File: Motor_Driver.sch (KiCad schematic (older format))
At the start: 42 parts, among them CN3 CONN_HEADER_R_A_2POS_2.5MM, Q14 AOD4185, Q5 2N7002BK, Q6 2N7002BK, Q7 2N7002BK, U7 LMC6772AIMX, U8 VNH5019ATR-E

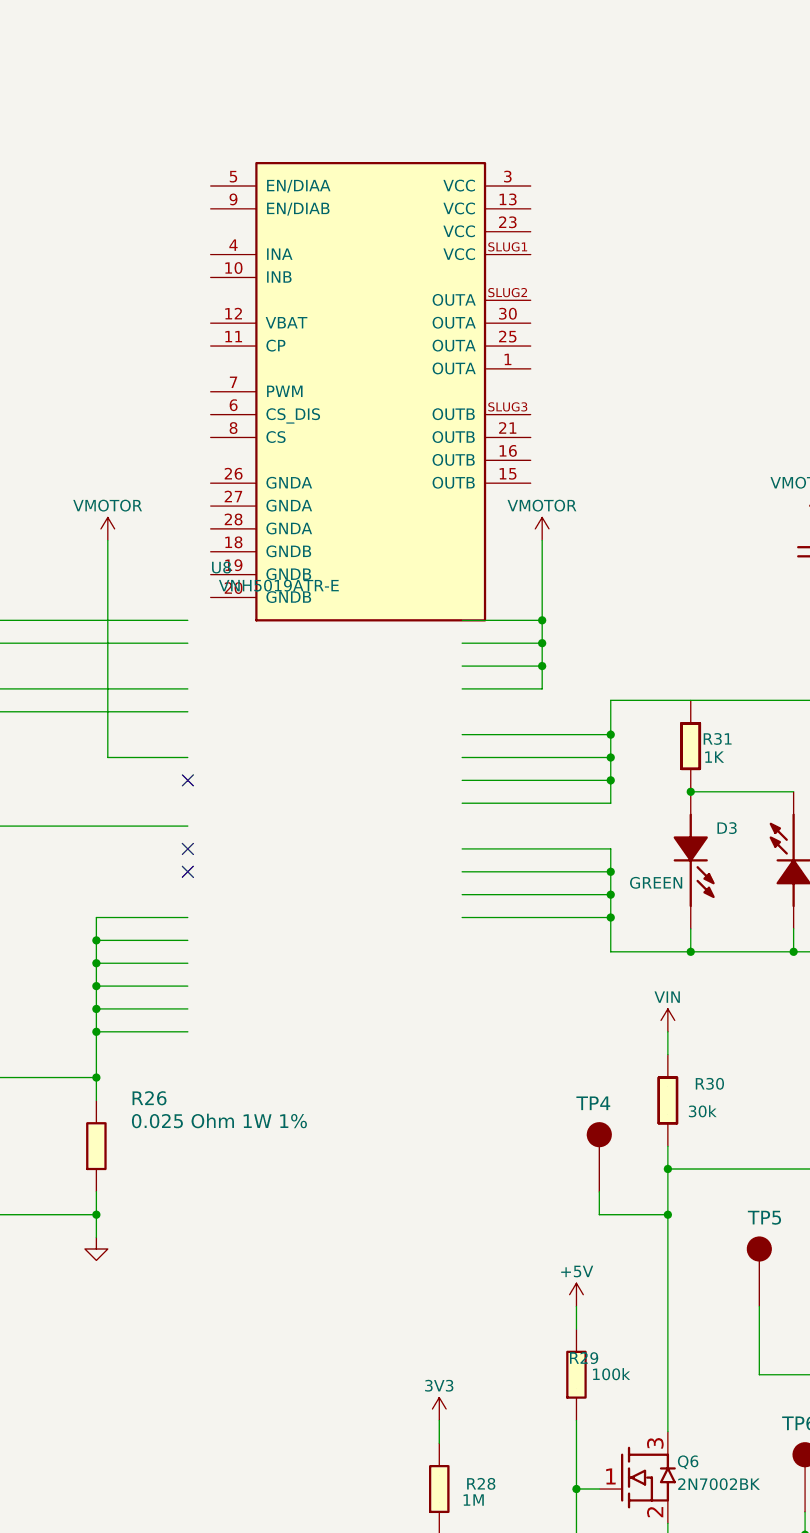
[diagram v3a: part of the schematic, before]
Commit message: Tweaked some issues on the battery charger page.
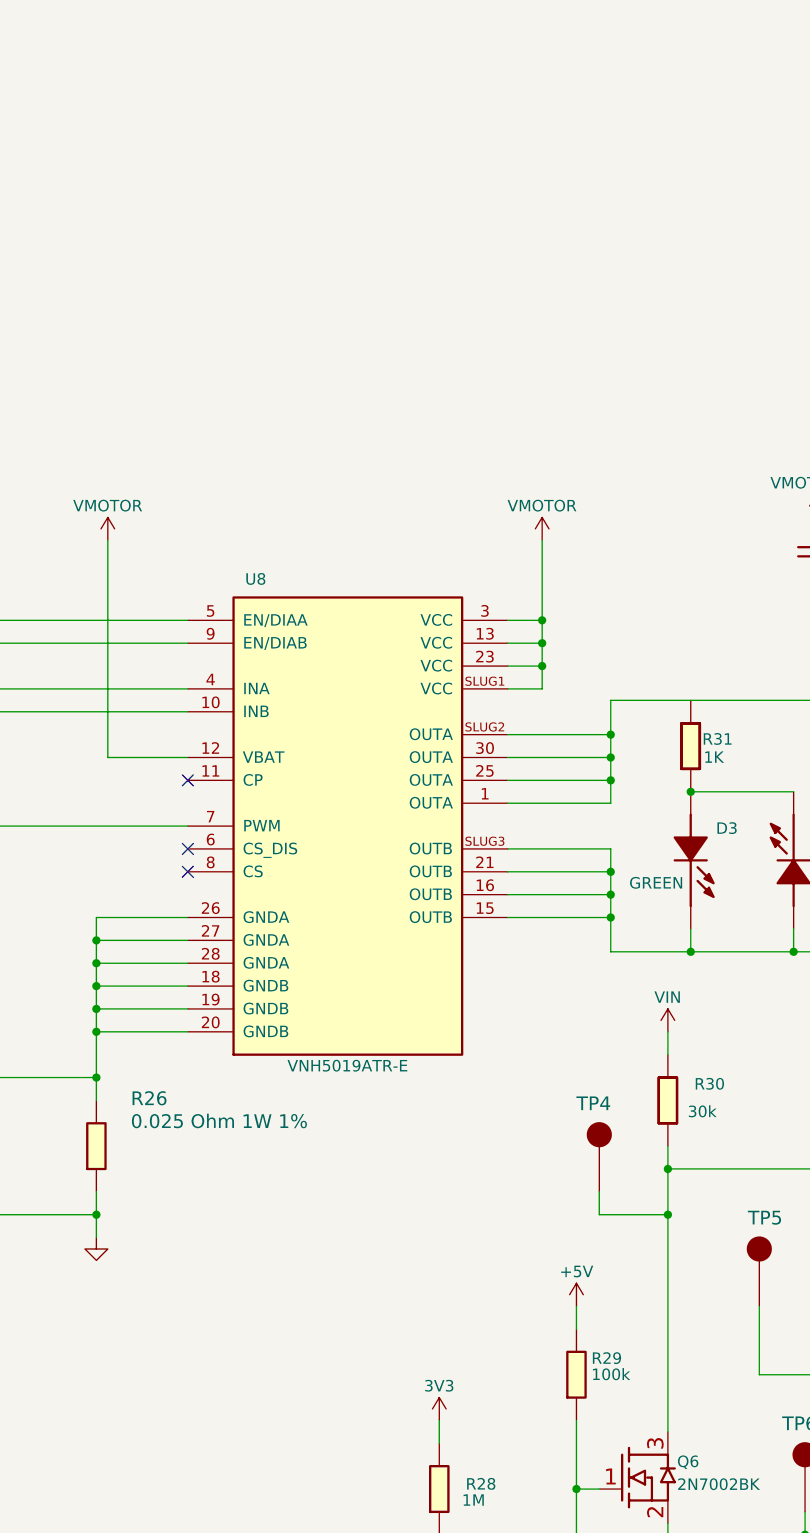
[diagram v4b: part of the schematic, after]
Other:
- moved on the sheet: U8
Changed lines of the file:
@@
 	4400 800  4400 1750
 Wire Wire Line
-	6600 2450 5950 2450
-Wire Wire Line
 	6600 2600 6600 2450
 Wire Wire Line
@@
 	8700 2050 8700 2600
 Wire Wire Line
-	6600 2350 5950 2350
-Wire Wire Line
-	6600 2250 5950 2250
-Wire Wire Line
-	6600 2150 5950 2150
-Wire Wire Line
 	6600 2250 6600 2150
 Wire Wire Line
@@
 	6600 2450 6600 2350
 Wire Wire Line
-	6600 1950 5950 1950
-Wire Wire Line
 	6600 1850 6600 1950
 Wire Wire Line
@@
 	6600 1650 6600 1750
 Wire Wire Line
-	6600 1850 5950 1850
-Wire Wire Line
-	6600 1750 5950 1750
-Wire Wire Line
-	6600 1650 5950 1650
-Wire Wire Line
 	6600 1500 6600 1650
 Wire Wire Line
 	8700 1950 8700 1500
 Wire Wire Line
-	6300 1450 5950 1450
-Wire Wire Line
 	6300 1350 6300 1450
 Wire Wire Line
@@
 Wire Wire Line
 	6300 800  6300 1150
-Wire Wire Line
-	6300 1350 5950 1350
-Wire Wire Line
-	6300 1250 5950 1250
-Wire Wire Line
-	6300 1150 5950 1150
 Wire Wire Line
 	7500 1150 7500 1000
@@
 L OpenVent:VNH5019ATR-E U8
 U 1 1 5F8DD116
-P 4850 1050
-F 0 "U8" H 4850 1150 50  0000 L BNN
-F 1 "VNH5019ATR-E" H 5150 1100 50  0000 C CNN
-F 2 "Package_SO:ST_MultiPowerSO-30" H 4850 1050 50  0001 C CNN
-F 3 "http://www.st.com/content/ccc/resource/technical/document/datasheet/1c/26/60/a8/3e/70/4c/e1/CD00234623.pdf/files/CD00234623.pdf/jcr:content/translations/en.CD00234623.pdf" H 4850 1050 60  0001 C CNN
-F 4 "STMicroelectronics" H 4850 1050 50  0001 C CNN "Mfr"
-F 5 "VNH5019ATR-E" H 4850 1050 50  0001 C CNN "Mfr_PN"
-F 6 "IC MTR DRV 5.5-24V MULTIPWRSO-30" H 4850 1050 50  0001 C CNN "Desc"
-F 7 "Motor Driver Power MOSFET Parallel, PWM MultiPowerSO-30" H 4850 1050 50  0001 C CNN "Detailed"
-F 8 "DigiKey" H 4850 1050 50  0001 C CNN "DistName"
-F 9 "497-13073-2-ND" H 4850 1050 50  0001 C CNN "Dist_PN"
-	1    4850 1050
+P 4750 2950
+F 0 "U8" H 5000 4900 50  0000 L BNN
+F 1 "VNH5019ATR-E" H 5450 2800 50  0000 C CNN
+F 2 "Package_SO:ST_MultiPowerSO-30" H 4750 2950 50  0001 C CNN
+F 3 "http://www.st.com/content/ccc/resource/technical/document/datasheet/1c/26/60/a8/3e/70/4c/e1/CD00234623.pdf/files/CD00234623.pdf/jcr:content/translations/en.CD00234623.pdf" H 4750 2950 60  0001 C CNN
+F 4 "STMicroelectronics" H 4750 2950 50  0001 C CNN "Mfr"
+F 5 "VNH5019ATR-E" H 4750 2950 50  0001 C CNN "Mfr_PN"
+F 6 "IC MTR DRV 5.5-24V MULTIPWRSO-30" H 4750 2950 50  0001 C CNN "Desc"
+F 7 "Motor Driver Power MOSFET Parallel, PWM MultiPowerSO-30" H 4750 2950 50  0001 C CNN "Detailed"
+F 8 "DigiKey" H 4750 2950 50  0001 C CNN "DistName"
+F 9 "497-13073-2-ND" H 4750 2950 50  0001 C CNN "Dist_PN"
+	1    4750 2950
 	1    0    0    -1
 $EndComp
@@
 U 1 1 5F8DD0FC
 P 6350 4550
-F 0 "R29" V 6550 4350 50  0000 L BNN
+F 0 "R29" V 6550 4250 50  0000 L BNN
 F 1 "100K_0603_Chip_Resistor,_1%,_0.1W" V 6350 4400 50  0001 C CNN
 F 2 "Resistor_SMD:R_0603_1608Metric" H 6250 4410 50  0001 C CNN
@@
 	1    0    0    -1
 $EndComp
+Wire Wire Line
+	6300 1450 6150 1450
+Wire Wire Line
+	6600 1950 6150 1950
+Wire Wire Line
+	6600 2150 6150 2150
+Wire Wire Line
+	6300 1350 6150 1350
+Wire Wire Line
+	6300 1250 6150 1250
+Wire Wire Line
+	6300 1150 6150 1150
+Wire Wire Line
+	6600 2450 6150 2450
+Wire Wire Line
+	6600 2350 6150 2350
+Wire Wire Line
+	6600 2250 6150 2250
+Wire Wire Line
+	6600 1850 6150 1850
+Wire Wire Line
+	6600 1750 6150 1750
+Wire Wire Line
+	6600 1650 6150 1650
 $EndSCHEMATC

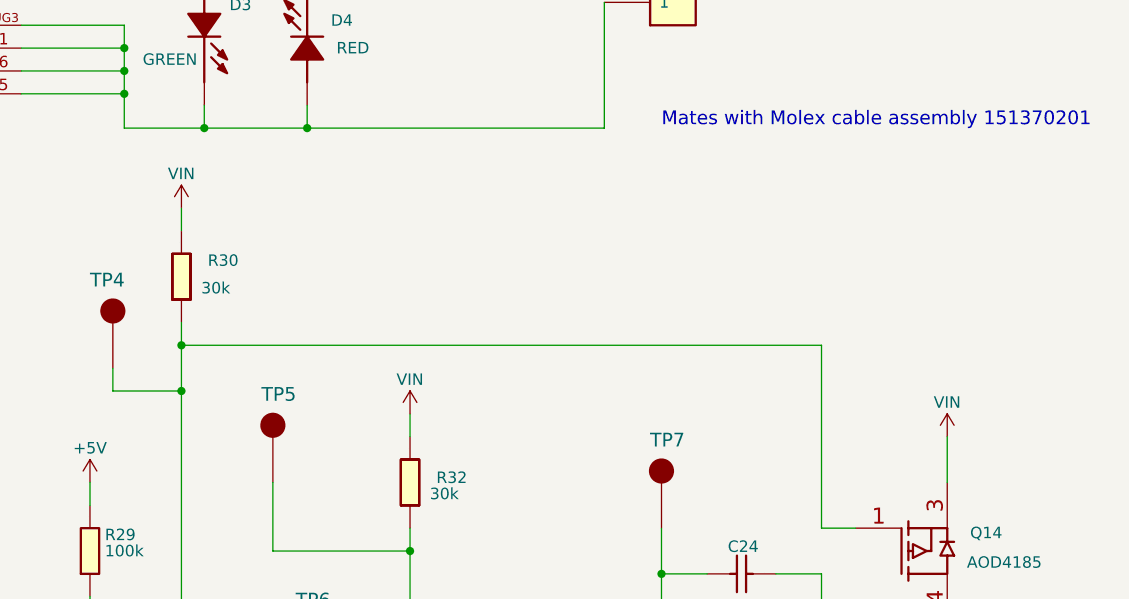
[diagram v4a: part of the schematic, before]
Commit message: Battery Charger page mostly finished, might want to think about what to do with the battery charging current signal (it's analog).
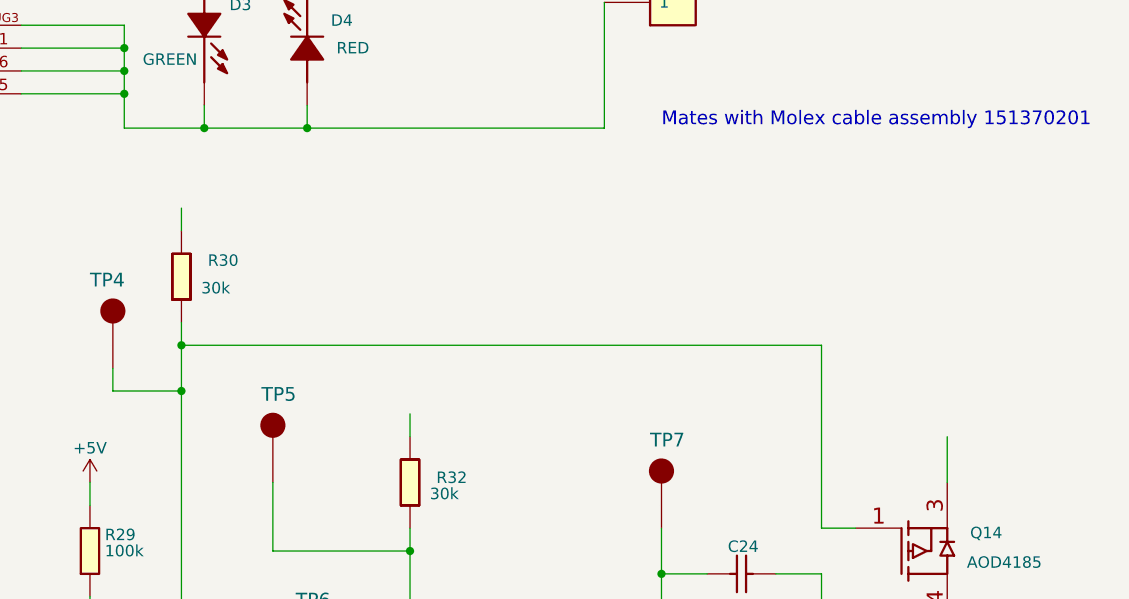
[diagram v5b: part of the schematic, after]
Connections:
- removed net VIN: Q14.3 (Source), R30.2, R32.2
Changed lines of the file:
@@
-$EndComp
-$Comp
-L OpenVent:VIN #VIN_02
-U 1 1 5F8DD127
-P 7850 3850
-F 0 "#VIN_02" H 7850 3850 20  0001 C CNN
-F 1 "VIN" H 7850 4000 50  0000 C CNN
-F 2 "" H 7850 3850 70  0000 C CNN
-F 3 "" H 7850 3850 70  0000 C CNN
-	1    7850 3850
-	1    0    0    -1
-$EndComp
-$Comp
-L OpenVent:VIN #VIN_03
-U 1 1 5F8DD126
-P 10200 3950
-F 0 "#VIN_03" H 10200 3950 20  0001 C CNN
-F 1 "VIN" H 10200 4100 50  0000 C CNN
-F 2 "" H 10200 3950 70  0000 C CNN
-F 3 "" H 10200 3950 70  0000 C CNN
-	1    10200 3950
-	1    0    0    -1
 $EndComp
 $Comp
@@
 	1    0    0    -1
 $EndComp
-$Comp
-L OpenVent:VIN #VIN_01
-U 1 1 5F8DD11E
-P 6850 2950
-F 0 "#VIN_01" H 6850 2950 20  0001 C CNN
-F 1 "VIN" H 6850 3100 50  0000 C CNN
-F 2 "" H 6850 2950 70  0000 C CNN
-F 3 "" H 6850 2950 70  0000 C CNN
-	1    6850 2950
-	1    0    0    -1
-$EndComp

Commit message: Split the design into two boards, main controller board and a power supply board.
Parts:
- removed C21: 470pF_0603_Ceramic_Capacitor,_5%,_100V,_C0G, Capacitor_SMD:C_0603_1608Metric, symbol OpenVent:470pF_0603_Ceramic_Capacitor,_5%,_100V,_C0G
- removed C22, C23: 1000uF_25V_Aluminium_SMD_Capacitor,_20%, Capacitor_SMD:CP_Elec_10x10, symbol OpenVent:1000uF_25V_Aluminium_SMD_Capacitor,_20%
- removed C24: 10nF_0603_Ceramic_Capacitor,_10%,_50V,_X7R-, Capacitor_SMD:C_0603_1608Metric, symbol OpenVent:10nF_0603_Ceramic_Capacitor,_10%,_50V,_X7R-
- removed CN3: CONN_HEADER_R_A_2POS_2.5MM, symbol OpenVent:CONN_HEADER_R_A_2POS_2.5MM
- removed D3: LED_GREEN_0603_SMD, LED_SMD:LED_0603_1608Metric, symbol OpenVent:LED_GREEN_0603_SMD
- removed D4: LED_Red_0603_SMD, LED_SMD:LED_0603_1608Metric, symbol OpenVent:LED_Red_0603_SMD
- removed D5: FSV20100V, Package_TO_SOT_SMD:TO-277A, symbol OpenVent:FSV20100V
- removed Q14: AOD4185, Package_TO_SOT_SMD:TO-252-2, symbol OpenVent:AOD4185
- removed Q5, Q6, Q7: 2N7002BK, Package_TO_SOT_SMD:SOT-23, symbol OpenVent:2N7002BK
- removed R16, R18, R27: 10k_0603_Chip_Resistor,_1%,_0.1W, Resistor_SMD:R_0603_1608Metric, symbol OpenVent:10k_0603_Chip_Resistor,_1%,_0.1W
- removed R17, R23: 215k_0603_Chip_Resistor,_1%,_0.1W, Resistor_SMD:R_0603_1608Metric, symbol OpenVent:215k_0603_Chip_Resistor,_1%,_0.1W
- removed R19, R20, R21, R22, R31: 1K_0603_Chip_Resistor,_1%,_0.1W, Resistor_SMD:R_0603_1608Metric, symbol OpenVent:1K_0603_Chip_Resistor,_1%,_0.1W
- removed R24, R25: 4k7_0603_Chip_Resistor,_1%,_0.1W, Resistor_SMD:R_0603_1608Metric, symbol OpenVent:4k7_0603_Chip_Resistor,_1%,_0.1W
- removed R26: 0.025 Ohm 1W 1%, Resistor_SMD:R_2010_5025Metric, symbol OpenVent:Resistor_2010_0.025OHM_sensing_1%_1W
- removed R28: 1M_0603_Chip_Resistor,_1%,_0.1W, Resistor_SMD:R_0603_1608Metric, symbol OpenVent:1M_0603_Chip_Resistor,_1%,_0.1W
- removed R29: 100K_0603_Chip_Resistor,_1%,_0.1W, Resistor_SMD:R_0603_1608Metric, symbol OpenVent:100K_0603_Chip_Resistor,_1%,_0.1W
- removed R30, R32, R35: 30k_0603_Chip_Resistor,_1%,_0.1W, Resistor_SMD:R_0603_1608Metric, symbol OpenVent:30k_0603_Chip_Resistor,_1%,_0.1W
- removed R33, R34: 20k_0603_Chip_Resistor,_1%,_0.1W, Resistor_SMD:R_0603_1608Metric, symbol OpenVent:20k_0603_Chip_Resistor,_1%,_0.1W
- removed R36: 0R1_0603_Chip_Resistor,_1%,_0.1W, Resistor_SMD:R_0603_1608Metric, symbol OpenVent:0R1_0603_Chip_Resistor,_1%,_0.1W
- removed TP1, TP2, TP3, TP4, TP5, TP6, TP7: Test_Point_PTH, TestPoint:TestPoint_Pad_2.0x2.0mm, symbol OpenVent:Test_Point_PTH
- removed U7: LMC6772AIMX, Package_SO:SO-8_3.9x4.9mm_P1.27mm, symbol OpenVent:LMC6772AIMX
- removed U8: VNH5019ATR-E, Package_SO:ST_MultiPowerSO-30, symbol OpenVent:VNH5019ATR-E
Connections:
- no-connect marks 4 -> 0
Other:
- note removed: "Bias Voltage Circuit still needs to be defined"
- note removed: "Mates with Molex cable assembly 151370201"
